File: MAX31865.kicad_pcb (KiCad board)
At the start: 2 copper layers, 25.4 x 27.9 mm, 23 parts, among them J1 connector, J2 Screw_Terminal_01x04, U1 MAX31865, U2 MIC5225

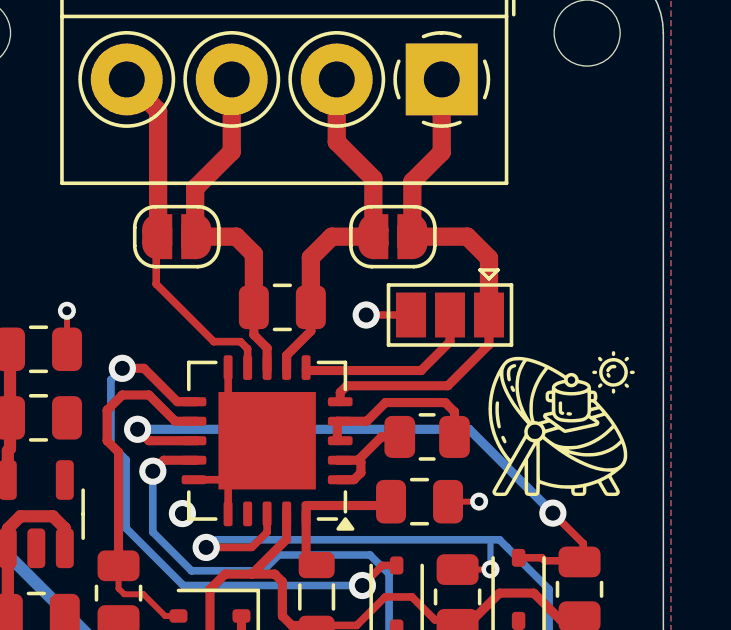
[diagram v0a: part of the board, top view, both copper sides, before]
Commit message: updated solder jumper
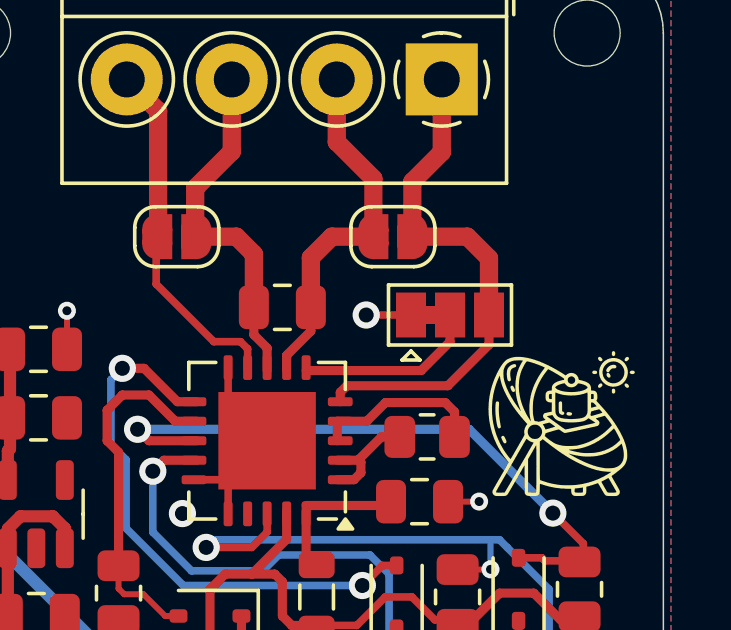
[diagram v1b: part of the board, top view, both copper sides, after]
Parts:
- JP1: renamed from SJ1; value SOLDERJUMPER_2WAY -> SolderJumper_3_Bridged12; footprint Jumper:SolderJumper-3_P1.3mm_Open_Pad1.0x1.5mm -> Jumper:SolderJumper-3_P1.3mm_Bridged12_Pad1.0x1.5mm
- turned JP1 to 0 degrees
- renumbered SJ3 to JP2, SJ4 to JP3
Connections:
- JP1 pad 1: Net-(J2-Pin_1) -> GND
- JP1 pad 3: GND -> Net-(J2-Pin_1)
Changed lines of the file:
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@@
 	(net 12 "Net-(U1-BIAS)")
 	(net 13 "Net-(U1-ISENSOR)")
-	(net 14 "Net-(SJ1-C)")
+	(net 14 "Net-(JP1-C)")
 	(net 15 "VIN")
 	(net 16 "unconnected-(U1-NC-Pad17)")
@@
 		)
 	)
-	(footprint "Jumper:SolderJumper-3_P1.3mm_Open_Pad1.0x1.5mm"
+	(footprint "Jumper:SolderJumper-3_P1.3mm_Bridged12_Pad1.0x1.5mm"
 		(layer "F.Cu")
-		(at 154.0891 102.9716 180)
-		(descr "SMD Solder 3-pad Jumper, 1x1.5mm Pads, 0.3mm gap, open")
-		(tags "solder jumper open")
-		(property "Reference" "SJ1"
-			(at 0 -1.8 180)
+		(at 154.0891 102.9716)
+		(descr "SMD Solder 3-pad Jumper, 1x1.5mm Pads, 0.3mm gap, pads 1-2 bridged with 1 copper strip")
+		(tags "net tie solder jumper bridged")
+		(property "Reference" "JP1"
+			(at 0 -1.8 0)
 			(layer "F.SilkS")
 			(hide yes)
@@
 			)
 		)
-		(property "Value" "SOLDERJUMPER_2WAY"
-			(at 0 2 180)
+		(property "Value" "SolderJumper_3_Bridged12"
+			(at 0 2 0)
 			(layer "F.Fab")
 			(effects
@@
 			)
 		)
-		(property "Footprint" "Jumper:SolderJumper-3_P1.3mm_Open_Pad1.0x1.5mm"
-			(at 0 0 180)
+		(property "Footprint" "Jumper:SolderJumper-3_P1.3mm_Bridged12_Pad1.0x1.5mm"
+			(at 0 0 0)
 			(unlocked yes)
 			(layer "F.Fab")
@@
 		)
 		(property "Datasheet" ""
-			(at 0 0 180)
+			(at 0 0 0)
 			(unlocked yes)
 			(layer "F.Fab")
@@
 			)
 		)
-		(property "Description" "Solder Jumper, 3-pole, open"
-			(at 0 0 180)
+		(property "Description" "3-pole Solder Jumper, pins 1+2 closed/bridged"
+			(at 0 0 0)
 			(unlocked yes)
 			(layer "F.Fab")
@@
 			)
 		)
-		(property "Component package type" ""
-			(at 0 0 180)
-			(unlocked yes)
-			(layer "F.Fab")
-			(hide yes)
-			(effects
-				(font
-					(size 1 1)
-					(thickness 0.15)
-				)
-			)
-		)
-		(property "MPN" ""
-			(at 0 0 180)
-			(unlocked yes)
-			(layer "F.Fab")
-			(hide yes)
-			(effects
-				(font
-					(size 1 1)
-					(thickness 0.15)
-				)
-			)
-		)
-		(property "Manufacturer" ""
-			(at 0 0 180)
-			(unlocked yes)
-			(layer "F.Fab")
-			(hide yes)
-			(effects
-				(font
-					(size 1 1)
-					(thickness 0.15)
-				)
-			)
-		)
-		(property "SPN" ""
-			(at 0 0 180)
-			(unlocked yes)
-			(layer "F.Fab")
-			(hide yes)
-			(effects
-				(font
-					(size 1 1)
-					(thickness 0.15)
-				)
-			)
-		)
-		(property "Supplier" ""
-			(at 0 0 180)
-			(unlocked yes)
-			(layer "F.Fab")
-			(hide yes)
-			(effects
-				(font
-					(size 1 1)
-					(thickness 0.15)
-				)
-			)
-		)
-		(property ki_fp_filters "SolderJumper*Open*")
+		(property ki_fp_filters "SolderJumper*Bridged12*")
 		(sheetname "Root")
 		(sheetfile "MAX31865.kicad_sch")
 		(zone_connect 1)
 		(attr exclude_from_pos_files exclude_from_bom)
+		(net_tie_pad_groups "1, 2")
+		(fp_poly
+			(pts
+				(xy -0.9 -0.3) (xy -0.4 -0.3) (xy -0.4 0.3) (xy -0.9 0.3)
+			)
+			(stroke
+				(width 0)
+				(type solid)
+			)
+			(fill solid)
+			(layer "F.Cu")
+		)
 		(fp_line
-			(start 2.05 1)
-			(end -2.05 1)
+			(start -2.05 -1)
+			(end 2.05 -1)
 			(stroke
 				(width 0.12)
@@
 		)
 		(fp_line
-			(start 2.05 -1)
-			(end 2.05 1)
+			(start -2.05 1)
+			(end -2.05 -1)
 			(stroke
 				(width 0.12)
@@
 		)
 		(fp_line
-			(start -1.3 1.2)
+			(start -1.6 1.5)
 			(end -1 1.5)
 			(stroke
@@
 		)
 		(fp_line
-			(start -1.6 1.5)
+			(start -1.3 1.2)
 			(end -1 1.5)
 			(stroke
@@
 		)
 		(fp_line
-			(start -2.05 1)
-			(end -2.05 -1)
+			(start 2.05 -1)
+			(end 2.05 1)
 			(stroke
 				(width 0.12)
@@
 		)
 		(fp_line
-			(start -2.05 -1)
-			(end 2.05 -1)
+			(start 2.05 1)
+			(end -2.05 1)
 			(stroke
 				(width 0.12)
@@
 		)
 		(fp_line
-			(start 2.3 1.25)
-			(end 2.3 -1.25)
+			(start -2.3 -1.25)
+			(end -2.3 1.25)
 			(stroke
 				(width 0.05)
@@
 		)
 		(fp_line
-			(start 2.3 1.25)
-			(end -2.3 1.25)
+			(start -2.3 -1.25)
+			(end 2.3 -1.25)
 			(stroke
 				(width 0.05)
@@
 		)
 		(fp_line
-			(start -2.3 -1.25)
-			(end 2.3 -1.25)
+			(start 2.3 1.25)
+			(end -2.3 1.25)
 			(stroke
 				(width 0.05)
@@
 		)
 		(fp_line
-			(start -2.3 -1.25)
-			(end -2.3 1.25)
+			(start 2.3 1.25)
+			(end 2.3 -1.25)
 			(stroke
 				(width 0.05)
@@
 			(layer "F.CrtYd")
 		)
-		(fp_text user "3"
-			(at 2.54 0.635 180)
-			(layer "F.Fab")
-			(effects
-				(font
-					(size 1.1684 1.1684)
-					(thickness 0.1016)
-				)
-				(justify left bottom)
-			)
-		)
-		(fp_text user "1"
-			(at -3.302 0.635 180)
-			(layer "F.Fab")
-			(effects
-				(font
-					(size 1.1684 1.1684)
-					(thickness 0.1016)
-				)
-				(justify left bottom)
-			)
-		)
 		(pad "1" smd rect
-			(at -1.3 0 180)
+			(at -1.3 0)
 			(size 1 1.5)
 			(layers "F.Cu" "F.Mask")
-			(net 21 "Net-(J2-Pin_1)")
+			(net 1 "GND")
 			(pinfunction "A")
 			(pintype "passive")
 		)
 		(pad "2" smd rect
-			(at 0 0 180)
+			(at 0 0)
 			(size 1 1.5)
 			(layers "F.Cu" "F.Mask")
-			(net 14 "Net-(SJ1-C)")
+			(net 14 "Net-(JP1-C)")
 			(pinfunction "C")
 			(pintype "passive")
 		)
 		(pad "3" smd rect
-			(at 1.3 0 180)
+			(at 1.3 0)
 			(size 1 1.5)
 			(layers "F.Cu" "F.Mask")
-			(net 1 "GND")
+			(net 21 "Net-(J2-Pin_1)")
 			(pinfunction "B")
 			(pintype "passive")
@@
 		(descr "SMD Solder Jumper, 1x1.5mm, rounded Pads, 0.3mm gap, open")
 		(tags "solder jumper open")
-		(property "Reference" "SJ4"
+		(property "Reference" "JP3"
 			(at 0 -1.8 0)
 			(layer "F.SilkS")
@@
 			(layers "F.Cu" "F.Paste" "F.Mask")
 			(roundrect_rratio 0.25)
-			(net 14 "Net-(SJ1-C)")
+			(net 14 "Net-(JP1-C)")
 			(pinfunction "FORCE2")
 			(pintype "input")
@@
 		(descr "SMD Solder Jumper, 1x1.5mm, rounded Pads, 0.3mm gap, open")
 		(tags "solder jumper open")
-		(property "Reference" "SJ3"
+		(property "Reference" "JP2"
 			(at 0 -1.8 0)
 			(layer "F.SilkS")
@@
 		(tags "Through hole pin header THT 1x08 2.54mm single row")
 		(property "Reference" "J1"
-			(at 0 2.33 270)
+			(at 0 2.33 -90)
 			(layer "B.SilkS")
 			(hide yes)
@@
 		)
 		(property "Value" "connector"
-			(at 0 -20.11 270)
+			(at 0 -20.11 -90)
 			(layer "B.Fab")
 			(effects
@@
 		)
 		(fp_text user "${REFERENCE}"
-			(at 0 -8.89 360)
+			(at 0 -8.89 0)
 			(layer "B.Fab")
 			(effects

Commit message: fixed connection mistake
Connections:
- R6 pad 1: /DRDY -> Net-(D1-A)
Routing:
- net Net-(D1-A): track 18.7 -> 20.8 mm
- net /DRDY: track 21.4 -> 19.4 mm, vias 2 -> 1
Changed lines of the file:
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@@
 			(layers "F.Cu" "F.Paste" "F.Mask")
 			(roundrect_rratio 0.243902)
-			(net 11 "/DRDY")
+			(net 4 "Net-(D1-A)")
 			(pintype "passive")
 		)
@@
 	)
 	(segment
+		(start 154.2056 111.3196)
+		(end 154.3431 111.4571)
+		(width 0.254)
+		(layer "F.Cu")
+		(net 4)
+	)
+	(segment
+		(start 152.3111 111.3196)
+		(end 154.2056 111.3196)
+		(width 0.254)
+		(layer "F.Cu")
+		(net 4)
+	)
+	(segment
 		(start 143.1671 104.7496)
 		(end 143.8896 104.7496)
@@
 	)
 	(segment
-		(start 155.4329 111.4571)
-		(end 155.44 111.45)
-		(width 0.2)
-		(layer "F.Cu")
-		(net 11)
-	)
-	(segment
-		(start 154.3431 111.4571)
-		(end 155.4329 111.4571)
-		(width 0.2)
-		(layer "F.Cu")
-		(net 11)
-	)
-	(segment
 		(start 147.9931 110.2106)
 		(end 147.4851 110.7186)
@@
 		(net 11)
 	)
-	(via
-		(at 155.44 111.45)
-		(size 0.6)
-		(drill 0.3)
-		(layers "F.Cu" "B.Cu")
-		(net 11)
-	)
 	(segment
 		(start 146.2151 110.4646)
@@
 		(layer "B.Cu")
 		(net 11)
-	)
-	(segment
-		(start 155.44 111.45)
-		(end 155.44 110.4646)
-		(width 0.2)
-		(layer "B.Cu")
-		(net 11)

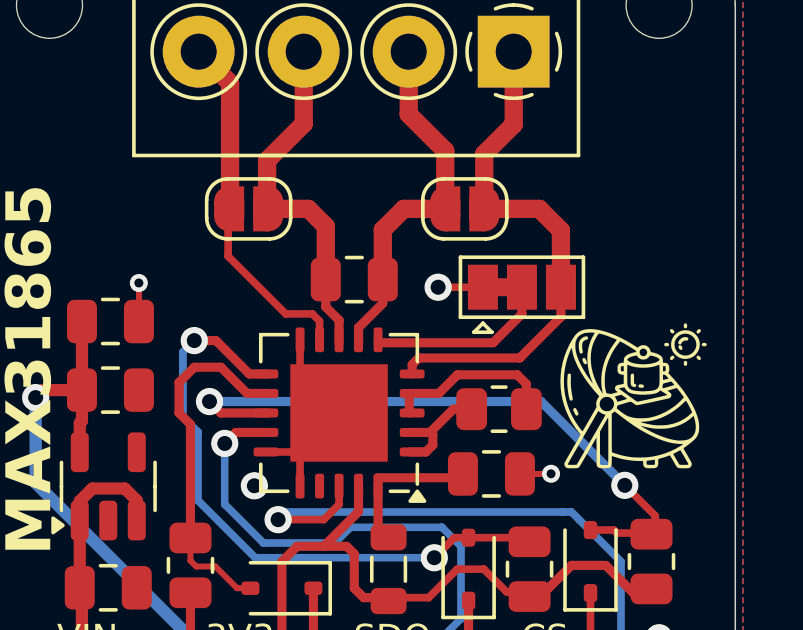
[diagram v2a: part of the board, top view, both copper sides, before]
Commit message: schematic update
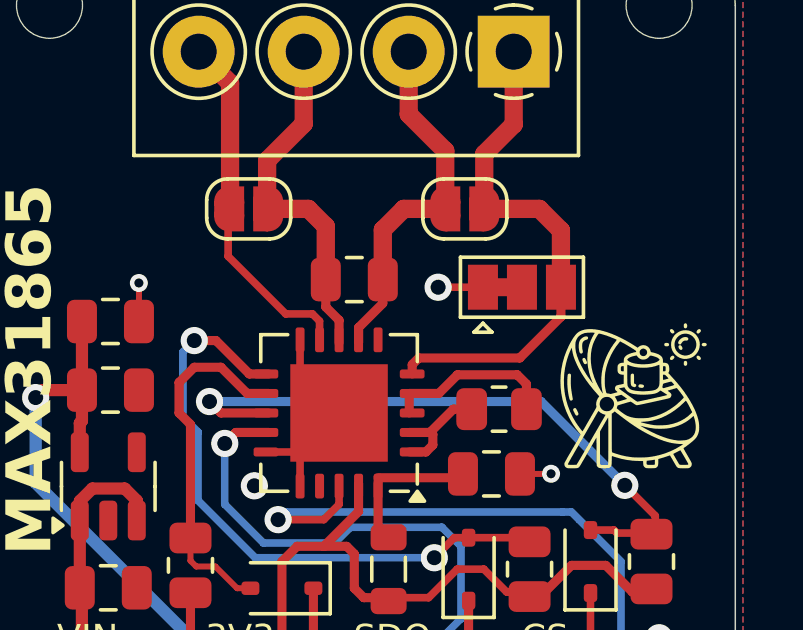
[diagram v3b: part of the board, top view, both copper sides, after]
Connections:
- JP1 pad 2: Net-(JP1-C) -> GND
- U1 pad 6: Net-(JP1-C) -> GND
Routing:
- net Net-(JP1-C): track 6.08 -> 0.00 mm

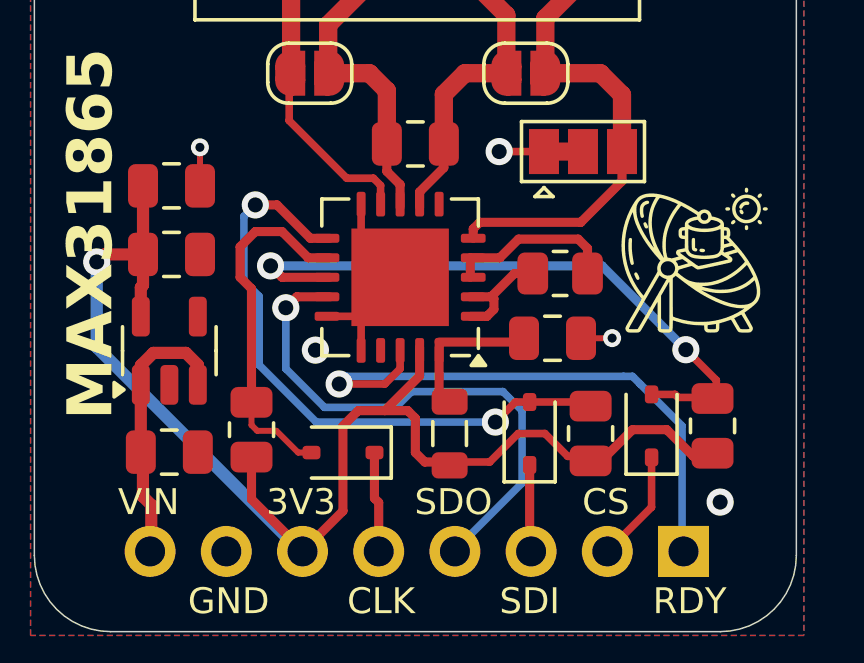
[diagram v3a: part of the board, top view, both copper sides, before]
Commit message: implemented Eurocircuits design remarks
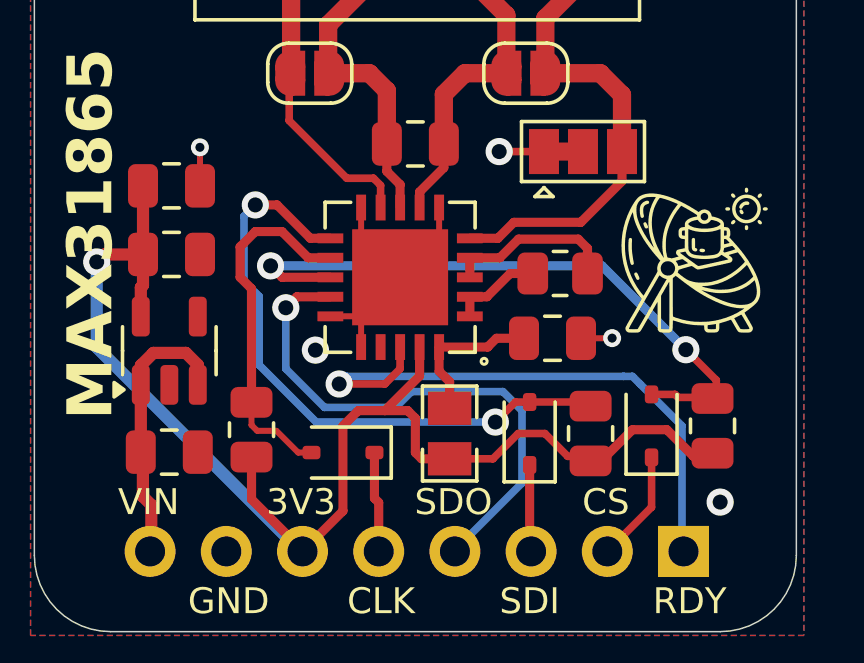
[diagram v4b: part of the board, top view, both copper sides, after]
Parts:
- FB1: footprint Inductor_SMD:L_0805_2012Metric -> external_footprints:LI0805G201R-10
- U1: footprint Package_DFN_QFN:TQFN-20-1EP_5x5mm_P0.65mm_EP3.25x3.25mm -> external_footprints:MAX31865ATP+
- turned U1 to 90 degrees
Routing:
- net Net-(U1-BIAS): track 3.71 -> 3.03 mm
- net GND: track 10.8 -> 10.3 mm
